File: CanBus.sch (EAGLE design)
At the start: 3 parts, among them IC1 MCP2515-I/P, IC2 MCP2551-E/P, X1 MAC64L

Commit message: Can-Bus, Reset für den RasPi, Kleinere Optimierungen
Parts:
- added C1, C10, C2, C3, C6: 100nF, rcl:C-EU050-024X044
- added C4, C5, C7, C8: 22pF, rcl:C-EU050-024X044
- added IC3: MCP2515-I/P, mcp2515_2551_2562:MCP2515-I/P
- added J1: (no value), con-amp:555141-1
- added JP2: (no value), jumper:JP1E
- added Q1, Q2: 16MHz, crystal:CRYSTALHC49S
- added R1, R4: 4k7, rcl:R-EU_0204/5
- added R2, R3: 120R, rcl:R-EU_0204/5
- added U1, U2: MCP2562-E/P, mcp2515_2551_2562:MCP2562-E/P
- IC1: device MCP2515:MCP2515-I/P -> mcp2515_2551_2562:MCP2515-I/P
- IC2: value MCP2551-E/P -> MEGA8-P; device MCP2551:MCP2551-E/P -> atmel:MEGA8-P
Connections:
- net PI_RESET renamed !PI_RESET
- removed net GND_INT: X1.A29, X1.A3, X1.A6, X1.A8, X1.C29, X1.C3, X1.C6, X1.C8
- removed net RS485_A: X1.C26
- removed net RS495_B: X1.C27
- new net AT_RXCAN: IC3.RXCAN, U2.RXD
- new net AT_SPI_CS: IC2.PB2(SS/OC1B), IC3.CS
- new net AT_SPI_MISO: IC2.PB4(MISO), IC3.SO
- new net AT_SPI_MOSI: IC2.PB3(MOSI/OC2), IC3.SI
- new net AT_SPI_SCK: IC2.PB5(SCK), IC3.SCK
- new net AT_TXCAN: IC3.TXCAN, U2.TXD
- new net CANH: J1.2, R2.1, U1.CANH, U2.CANH, X1.C26
- new net CANH_2: J1.7, R3.1
- new net CANL: J1.1, R2.2, U1.CANL, U2.CANL, X1.C27
- new net CANL_2: J1.8, JP2.2
- new net GND: C1.2, C10.2, C2.2, C3.2, C4.2, C5.2, C6.2, C7.2, C8.2, IC1.VSS, IC2.GND, IC2.GND@1, IC3.VSS, J1.3, J1.6, U1.STBY, U1.VSS, U2.STBY, U2.VSS, X1.A29, X1.A3, X1.A6, X1.A8, X1.C29, X1.C3, X1.C6, X1.C8
- new net N$1: C4.1, IC1.OSC1, Q1.2
- new net N$2: IC1.RESET, R1.1
- new net N$3: JP2.1, R3.2
- new net N$4: C5.1, IC1.OSC2, Q1.1
- new net N$5: IC3.RESET, R4.1
- new net N$6: C7.1, IC3.OSC1, Q2.2
- new net N$7: C8.1, IC3.OSC2, Q2.1
- new net RXCAN: IC1.RXCAN, U1.RXD
- new net TXCAN: IC1.TXCAN, U1.TXD
- net +24V: now also J1.4, J1.5
- net +3,3V: now also C1.1, C3.1, IC1.VDD, R1.2, U1.VIO
- net +5V_EXT: now also C10.1, C2.1, C6.1, IC2.VCC@1, IC3.VDD, R4.2, U1.VDD, U2.VDD, U2.VIO
- net GPIO.25: now also IC1.INT
- net SPI_CE0: now also IC1.CS
- net SPI_MISO: now also IC1.SO
- net SPI_MOSI: now also IC1.SI
- net SPI_SCLK: now also IC1.SCK

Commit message: Diverse Anpassungen
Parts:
- IC1, IC3: value MCP2515-I/P -> MCP2515-I/SO; device mcp2515_2551_2562:MCP2515-I/P -> mcp2515_2551_2562:MCP2515-I/SO
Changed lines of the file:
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@@
 <part name="FRAME1" library="frames" deviceset="A4L-LOC" device=""/>
 <part name="X1" library="con-vg" deviceset="MAC64L" device=""/>
-<part name="IC1" library="mcp2515_2551_2562" deviceset="MCP2515" device="-I/P"/>
+<part name="IC1" library="mcp2515_2551_2562" deviceset="MCP2515" device="-I/SO" value="MCP2515-I/SO"/>
 <part name="J1" library="con-amp" deviceset="555141-1" device=""/>
 <part name="U1" library="mcp2515_2551_2562" deviceset="MCP2562" device="-E/P"/>
@@
 <part name="C5" library="rcl" deviceset="C-EU" device="050-024X044" value="22pF"/>
 <part name="IC2" library="atmel" deviceset="MEGA8-P" device=""/>
-<part name="IC3" library="mcp2515_2551_2562" deviceset="MCP2515" device="-I/P"/>
+<part name="IC3" library="mcp2515_2551_2562" deviceset="MCP2515" device="-I/SO" value="MCP2515-I/SO"/>
 <part name="C6" library="rcl" deviceset="C-EU" device="050-024X044" value="100nF"/>
 <part name="R4" library="rcl" deviceset="R-EU_" device="0204/5" value="4k7"/>

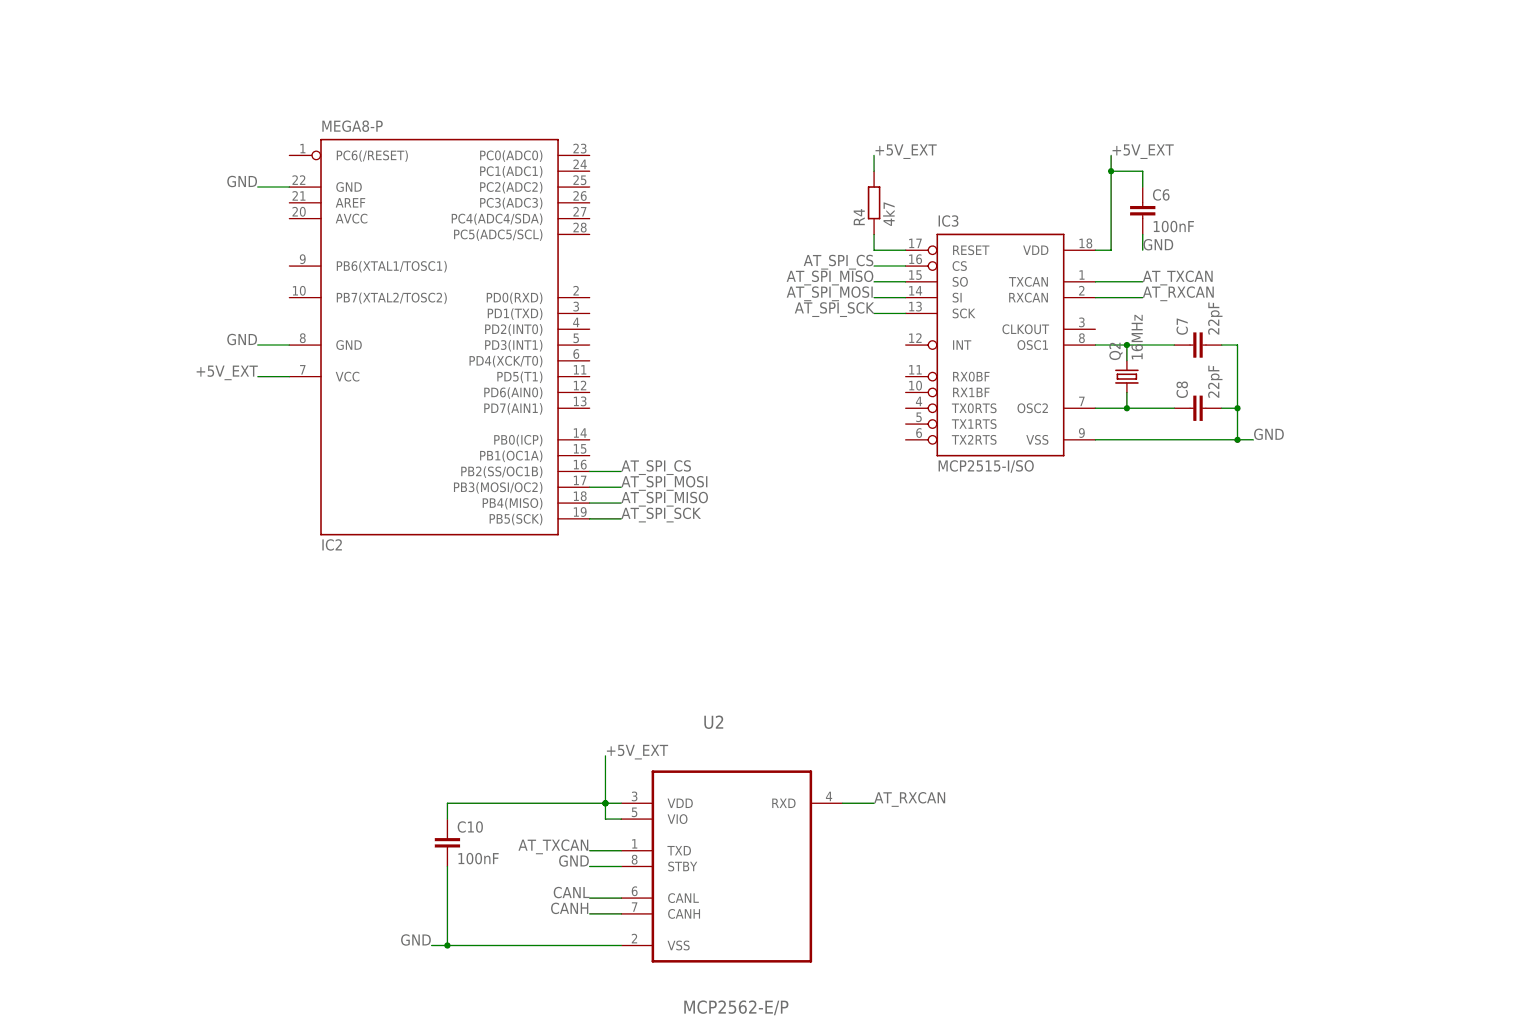
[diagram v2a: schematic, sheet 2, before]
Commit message: Pi, CanBus, Stromversorgung, Steckverbinder angepasst
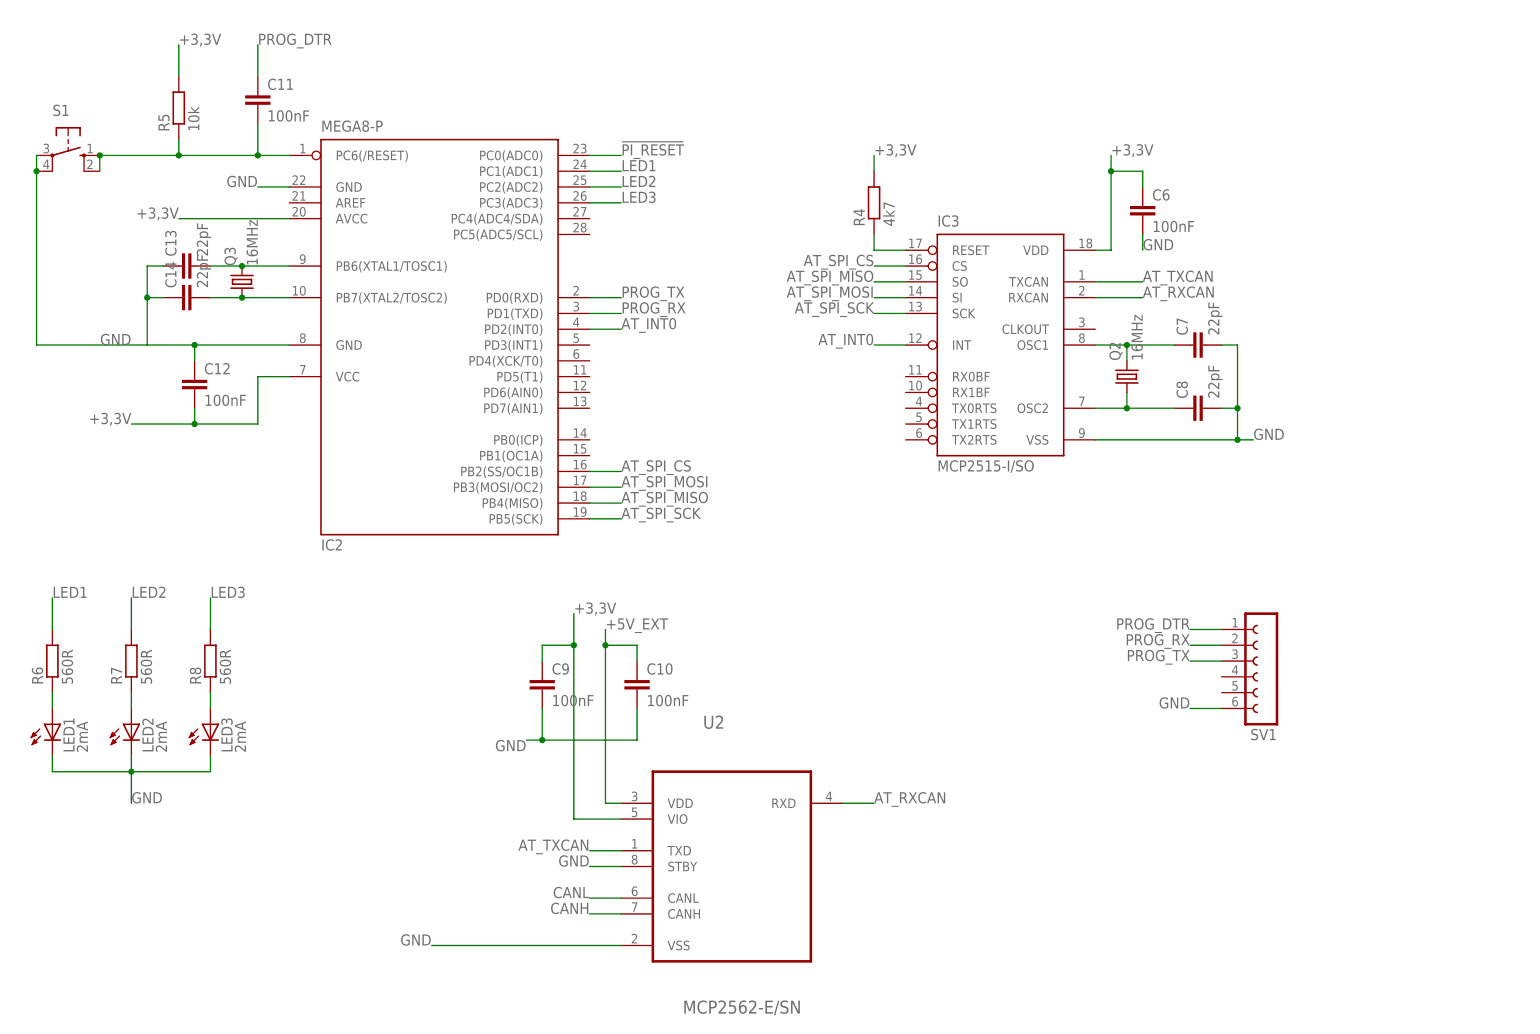
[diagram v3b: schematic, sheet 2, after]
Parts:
- added C11, C12, C9: 100nF, rcl:C-EUC1206
- added C13, C14: 22pF, rcl:C-EUC1206
- added LED1, LED2, LED3: 2mA, led:LED3MM
- added Q3: 16MHz, crystal:CRYSTALHC49UP
- added R5: 10k, rcl:R-EU_R1206
- added R6, R7, R8: 560R, rcl:R-EU_R1206
- added S1: (no value), switch-omron:10-XX
- added SV1: (no value), con-lsta:FE06W
- C1, C10, C2, C3, C4, C5, C6, C7, C8: device rcl:C-EU050-024X044 -> rcl:C-EUC1206
- J1: device con-amp:555141-1 -> mebp_8-8g:555141-1
- Q1, Q2: device crystal:CRYSTALHC49S -> crystal:CRYSTALHC49UP
- R1, R2, R3, R4: device rcl:R-EU_0204/5 -> rcl:R-EU_R1206
- U1, U2: value MCP2562-E/P -> MCP2562-E/SN; device mcp2515_2551_2562:MCP2562-E/P -> mcp2515_2551_2562:MCP2562-E/SN
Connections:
- new net AT_INT0: IC2.PD2(INT0), IC3.INT
- new net LED1: IC2.PC1(ADC1), R6.2
- new net LED2: IC2.PC2(ADC2), R7.2
- new net LED3: IC2.PC3(ADC3), R8.2
- new net N$10: C13.2, IC2.PB6(XTAL1/TOSC1), Q3.2
- new net N$11: C14.2, IC2.PB7(XTAL2/TOSC2), Q3.1
- new net N$12: C13.1, C14.1
- new net N$14: LED1.A, R6.1
- new net N$15: LED2.A, R7.1
- new net N$19: LED3.A, R8.1
- new net N$8: C11.2, IC2.PC6(/RESET), R5.1, S1.S, S1.S1
- new net PROG_DTR: C11.1, SV1.1
- new net PROG_RX: IC2.PD1(TXD), SV1.2
- new net PROG_TX: IC2.PD0(RXD), SV1.3
- net !PI_RESET: now also IC2.PC0(ADC0), X1.A26; no longer X1.C7
- net +3,3V: now also C12.2, C6.1, C9.1, IC2.AVCC, IC2.VCC@1, IC3.VDD, R4.2, R5.2, U2.VIO
- net +5V_EXT: no longer C6.1, IC2.VCC@1, IC3.VDD, R4.2, U2.VIO
- net CANH: no longer X1.C26
- net CANL: no longer X1.C27
- net GND: now also C12.1, C9.2, J1.S1, J1.S2, LED1.C, LED2.C, LED3.C, S1.P, S1.P1, SV1.6
- net GPIO.05: now also X1.C14; no longer X1.A14
- net GPIO.06: now also IC1.INT, X1.C15; no longer X1.A15
- net GPIO.12: now also X1.C16; no longer X1.A16
- net GPIO.13: now also X1.C17; no longer X1.A17
- net GPIO.16: now also X1.C18; no longer X1.A18
- net GPIO.17: now also X1.C19; no longer X1.A19
- net GPIO.18: now also X1.C20; no longer X1.A20
- net GPIO.19: now also X1.C21; no longer X1.A21
- net GPIO.20: now also X1.C22; no longer X1.A22
- net GPIO.21: now also X1.C23; no longer X1.A23
- net GPIO.22: now also X1.C24; no longer X1.A24
- net GPIO.23: now also X1.C25; no longer X1.A25
- net GPIO.24: now also X1.C26; no longer X1.A26
- net GPIO.25: now also X1.C27; no longer IC1.INT, X1.A27
- net RXD: now also X1.C12; no longer X1.C25
- net SPI_CE0: now also X1.A10; no longer X1.A12
- net SPI_CE1: now also X1.C11; no longer X1.A13
- net SPI_MISO: now also X1.A9; no longer X1.A10
- net SPI_MOSI: now also X1.C9; no longer X1.A9
- net SPI_SCLK: now also X1.C10; no longer X1.A11
- net TXD: now also X1.A12; no longer X1.C24
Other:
- moved on the sheet: C10

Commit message: Platinen angepasst, Backplane
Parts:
- added JP1, JP10, JP3, JP4, JP5, JP6, JP7, JP8, JP9: (no value), pinhead:PINHD-1X1
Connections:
- new net AT_PB0: IC2.PB0(ICP), JP9.1
- new net AT_PB1: IC2.PB1(OC1A), JP10.1
- new net AT_PC4: IC2.PC4(ADC4/SDA), JP1.1
- new net AT_PC5: IC2.PC5(ADC5/SCL), JP3.1
- new net AT_PD3: IC2.PD3(INT1), JP4.1
- new net AT_PD4: IC2.PD4(XCK/T0), JP5.1
- new net AT_PD5: IC2.PD5(T1), JP6.1
- new net AT_PD6: IC2.PD6(AIN0), JP7.1
- new net AT_PD7: IC2.PD7(AIN1), JP8.1
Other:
- moved on the sheet: C10, C6, C7, C8, C9, IC3, Q2, R4, SV1, U2

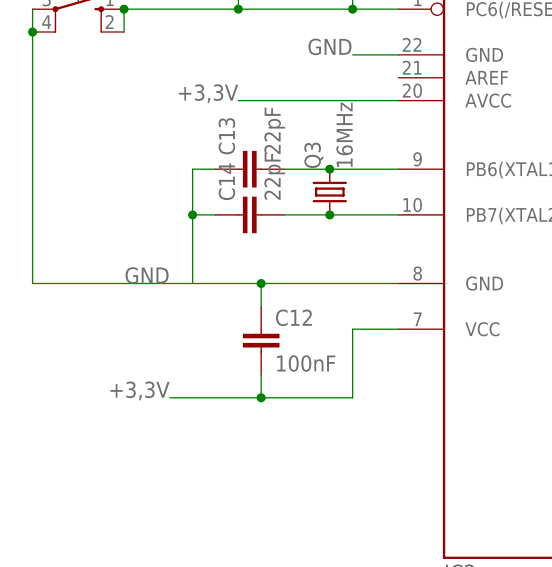
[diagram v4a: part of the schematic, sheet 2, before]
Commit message: Pi-Display hinzugefügt, Boards angepasst
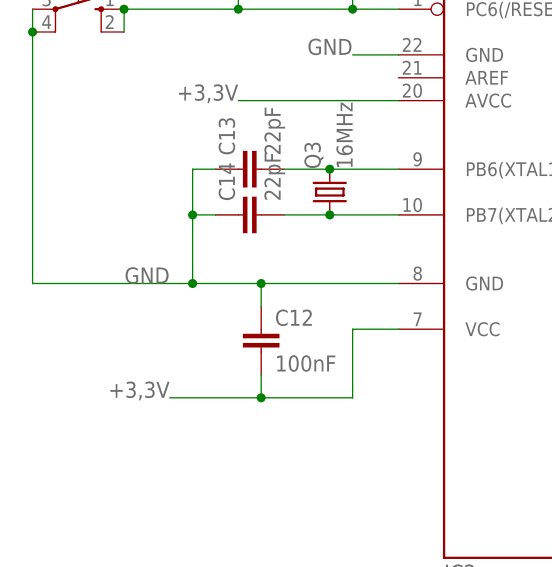
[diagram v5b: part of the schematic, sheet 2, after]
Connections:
- removed net N$12: C13.1, C14.1
- net GND: now also C13.1, C14.1
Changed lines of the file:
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@@
 <wire x1="10.16" y1="137.16" x2="10.16" y2="109.22" width="0.1524" layer="91"/>
 <junction x="10.16" y="137.16"/>
-<wire x1="10.16" y1="109.22" x2="35.56" y2="109.22" width="0.1524" layer="91"/>
+<wire x1="10.16" y1="109.22" x2="27.94" y2="109.22" width="0.1524" layer="91"/>
+<pinref part="C13" gate="G$1" pin="1"/>
+<wire x1="27.94" y1="109.22" x2="35.56" y2="109.22" width="0.1524" layer="91"/>
+<wire x1="30.48" y1="121.92" x2="27.94" y2="121.92" width="0.1524" layer="91"/>
+<wire x1="27.94" y1="121.92" x2="27.94" y2="116.84" width="0.1524" layer="91"/>
+<pinref part="C14" gate="G$1" pin="1"/>
+<wire x1="27.94" y1="116.84" x2="30.48" y2="116.84" width="0.1524" layer="91"/>
+<junction x="27.94" y="116.84"/>
+<wire x1="27.94" y1="116.84" x2="27.94" y2="109.22" width="0.1524" layer="91"/>
+<junction x="27.94" y="109.22"/>
 </segment>
 <segment>
@@
 </segment>
 </net>
-<net name="N$12" class="0">
-<segment>
-<pinref part="C13" gate="G$1" pin="1"/>
-<wire x1="30.48" y1="121.92" x2="27.94" y2="121.92" width="0.1524" layer="91"/>
-<wire x1="27.94" y1="121.92" x2="27.94" y2="116.84" width="0.1524" layer="91"/>
-<pinref part="C14" gate="G$1" pin="1"/>
-<wire x1="27.94" y1="116.84" x2="30.48" y2="116.84" width="0.1524" layer="91"/>
-<wire x1="27.94" y1="116.84" x2="27.94" y2="109.22" width="0.1524" layer="91"/>
-<junction x="27.94" y="116.84"/>
-</segment>
-</net>
